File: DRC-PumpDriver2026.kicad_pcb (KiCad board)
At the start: 2 copper layers, 80 x 60 mm, 89 parts, among them J1 STLINK, J10 Vin_PWR, J2 CAN, J3 CAN, J4 PUMP1, J5 PUMP2, J6 PUMP3, J7 PUMP4, J8 PUMP5, J9 PUMP6, Q1 MTB7D0N6RJ3, Q2 MTB7D0N6RJ3, Q3 MTB7D0N6RJ3, Q4 MTB7D0N6RJ3, Q5 MTB7D0N6RJ3, Q6 MTB7D0N6RJ3, SW1 SW_Push, SW2 DIP, U1 AZ1084C-3.3, U2 STM32F303K8Tx, U3 SI-8050Y, U4 TLP2348, U5 TLP2348, U6 TLP2348, U7 TLP2348, U8 TLP2348, U9 TLP2348

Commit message: シルクスクリーンを修正
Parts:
- D5: value 5V -> POWER
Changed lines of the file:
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@@
 			)
 		)
-		(property "Value" "5V"
+		(property "Value" "POWER"
 			(at -1.919 0 270)
 			(unlocked yes)

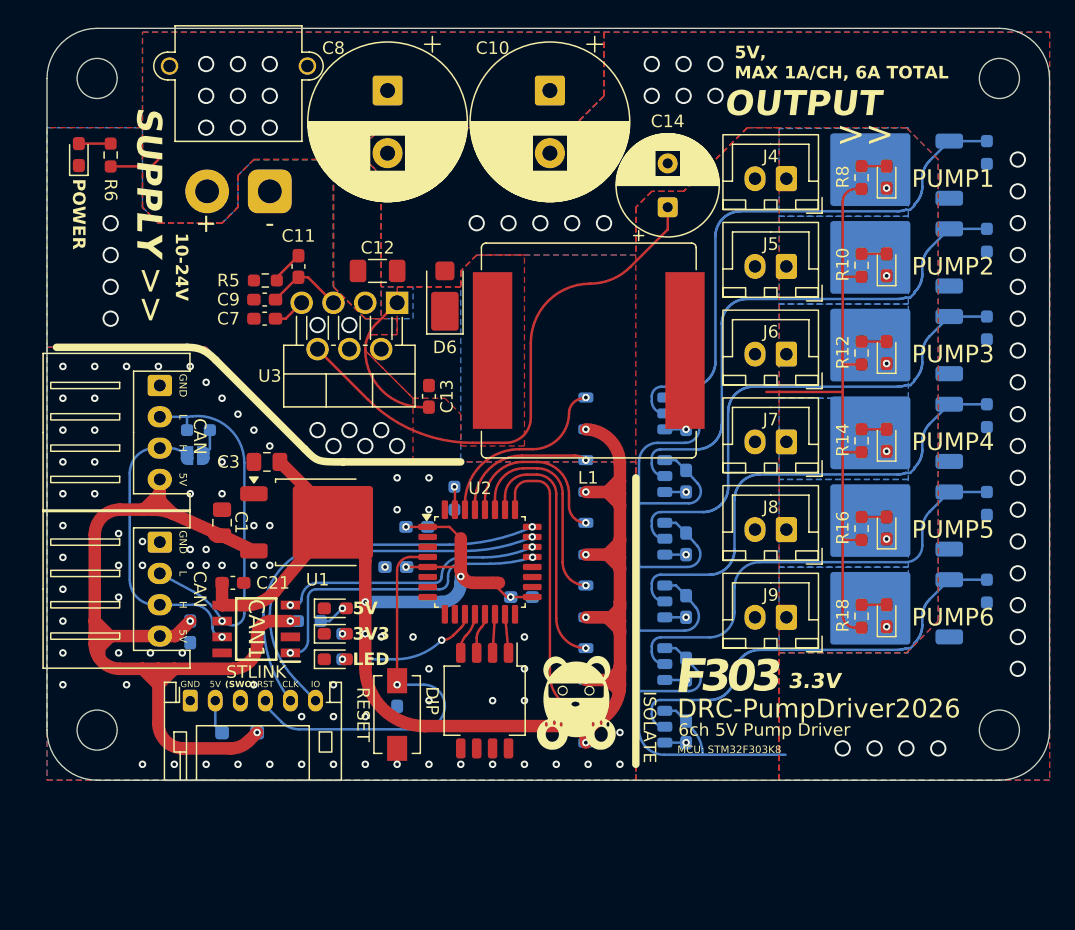
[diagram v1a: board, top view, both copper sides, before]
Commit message: 抜けてたフォトカプラの抵抗を追加
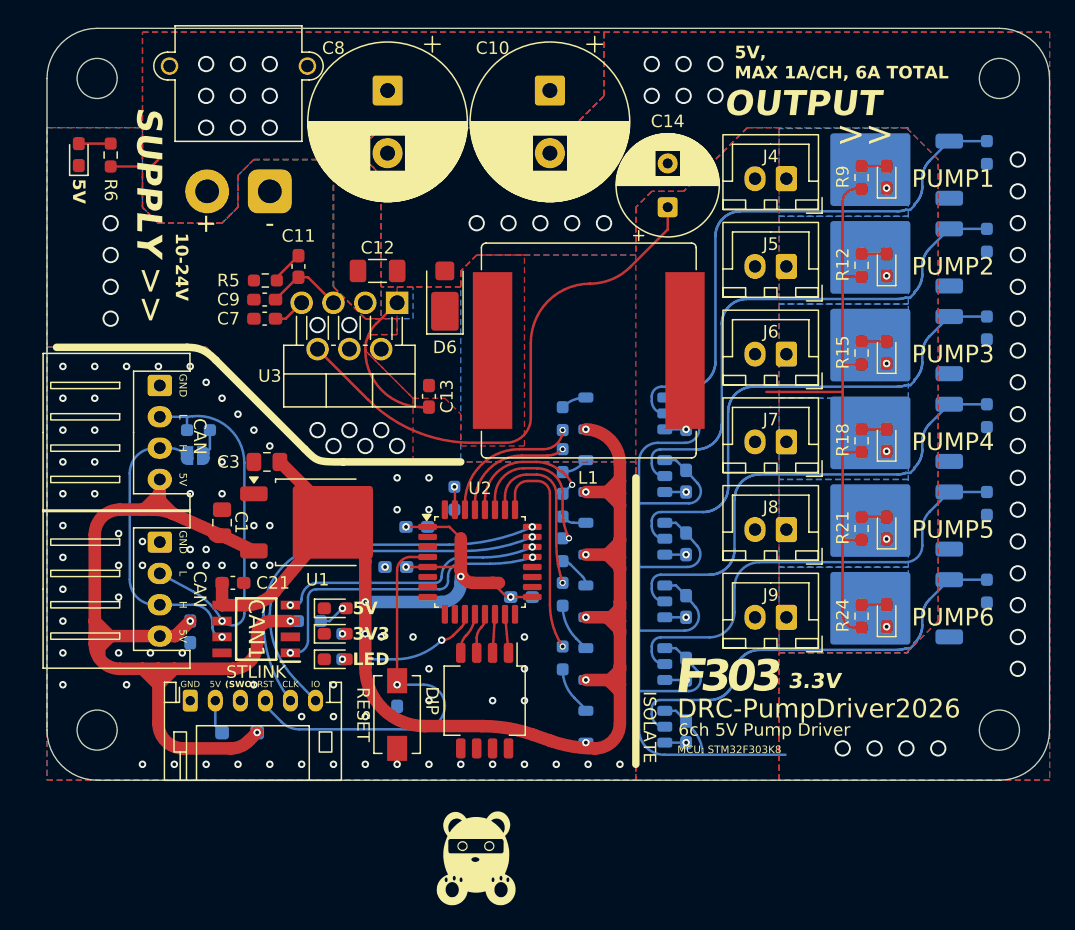
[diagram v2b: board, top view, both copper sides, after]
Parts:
- added R10: 560, Resistor_SMD:R_0603_1608Metric_Pad0.98x0.95mm_HandSolder, B.Cu at (154.2, 94.5)
- added R13: 560, Resistor_SMD:R_0603_1608Metric_Pad0.98x0.95mm_HandSolder, B.Cu at (154.2, 98.1)
- added R16: 560, Resistor_SMD:R_0603_1608Metric_Pad0.98x0.95mm_HandSolder, B.Cu at (154.2, 101.6)
- added R19: 560, Resistor_SMD:R_0603_1608Metric_Pad0.98x0.95mm_HandSolder, B.Cu at (154.2, 105.2)
- added R22: 560, Resistor_SMD:R_0603_1608Metric_Pad0.98x0.95mm_HandSolder, B.Cu at (154.2, 110.3)
- added R7: 560, Resistor_SMD:R_0603_1608Metric_Pad0.98x0.95mm_HandSolder, B.Cu at (154.2, 91.2)
- D5: value POWER -> 5V
- moved G*** 14.8 mm to (147.3, 126.4)
- renumbered R9 to R11, R10 to R12, R11 to R14, R12 to R15, R13 to R17, R14 to R18, R15 to R20, R16 to R21, R17 to R23, R18 to R24, R19 to R25, R7 to R8, R8 to R9
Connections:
- U4 pad 3: /PUMP1_EN -> Net-(U4-K)
- U5 pad 3: /PUMP2_EN -> Net-(U5-K)
- U6 pad 3: /PUMP3_EN -> Net-(U6-K)
- U7 pad 3: /PUMP4_EN -> Net-(U7-K)
- U8 pad 3: /PUMP5_EN -> Net-(U8-K)
- U9 pad 3: /PUMP6_EN -> Net-(U9-K)
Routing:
- net /PUMP6_EN: track 24.0 -> 17.5 mm
- net /PUMP5_EN: track 20.4 -> 14.0 mm
- net /PUMP4_EN: track 17.0 -> 12.3 mm
- net Net-(U8-K): track 0.00 -> 3.97 mm
- net Net-(U9-K): track 0.00 -> 3.91 mm
- net /PUMP1_EN: track 14.6 -> 11.4 mm
- net Net-(U7-K): track 0.00 -> 2.83 mm
- net /PUMP3_EN: track 13.5 -> 11.1 mm
- net Net-(U5-K): track 0.00 -> 2.14 mm
- net Net-(U4-K): track 0.00 -> 2.05 mm
- net Net-(U6-K): track 0.00 -> 2.01 mm
- net +3V3: track 135.0 -> 133.2 mm
- net /PUMP2_EN: track 11.5 -> 9.69 mm
- net GND: vias 80 -> 79
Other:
- board text added: "Designed by kotek, April 2026"
- board text removed: "Designed by kotek, March 2026"

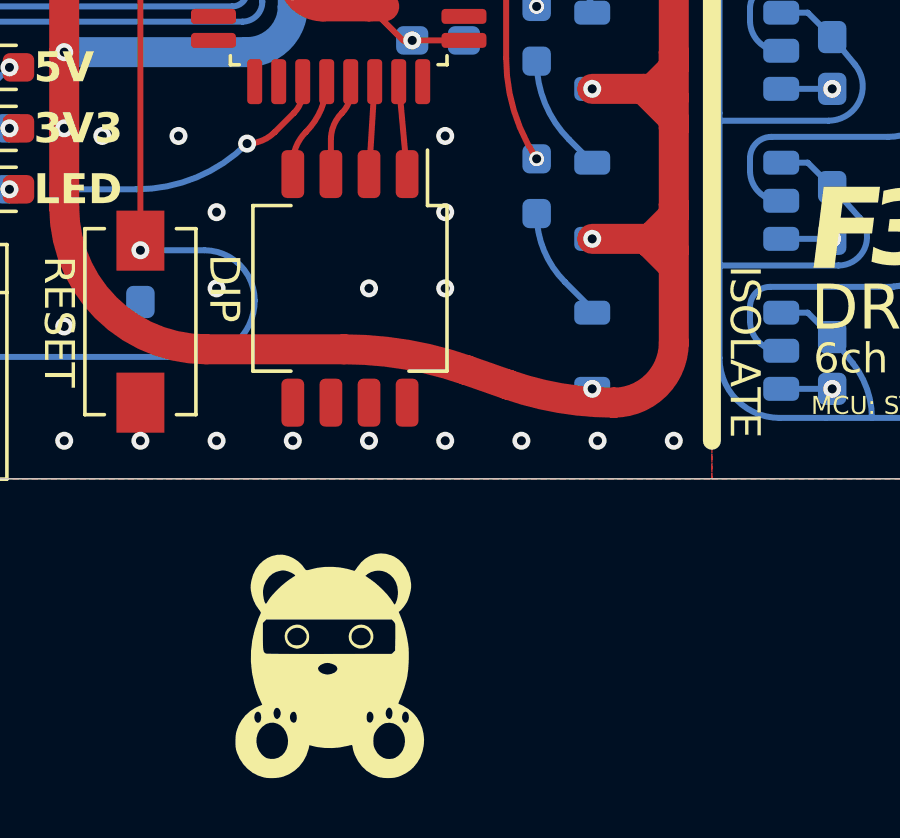
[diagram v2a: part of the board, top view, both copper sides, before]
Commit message: ロボクマのシルクスクリーンの位置を変更
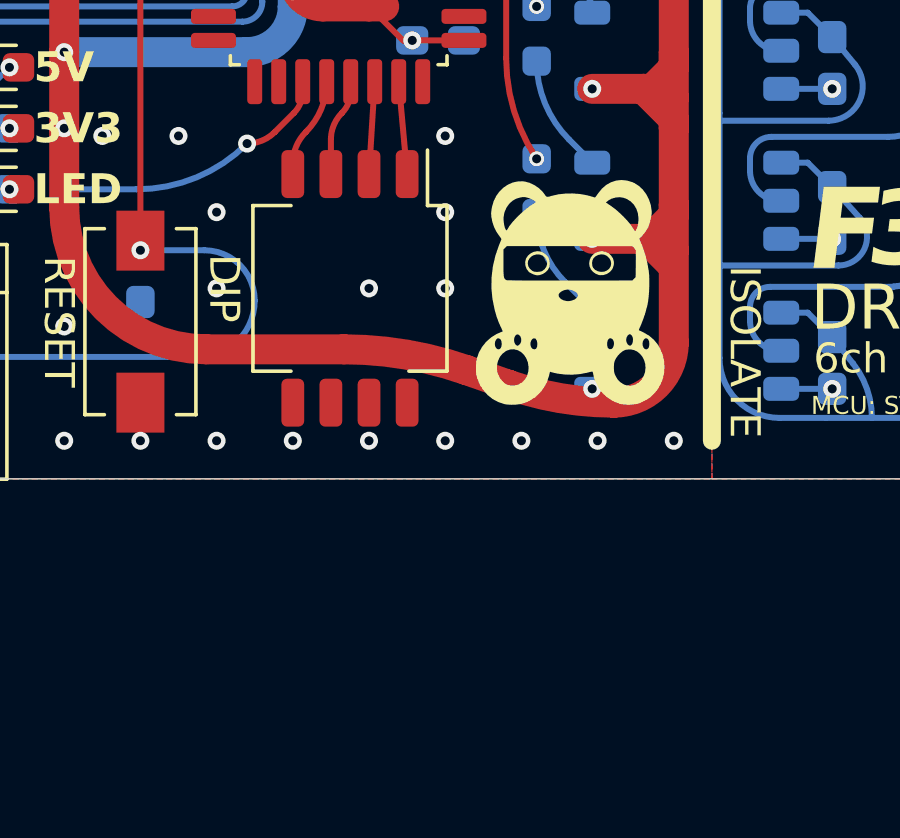
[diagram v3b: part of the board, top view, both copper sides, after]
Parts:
- moved G*** 14.8 mm to (155.3, 113.9)

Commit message: バージョン表記を追加
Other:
- board text added: "DRC-PumpDriver2026 v0.0.1"

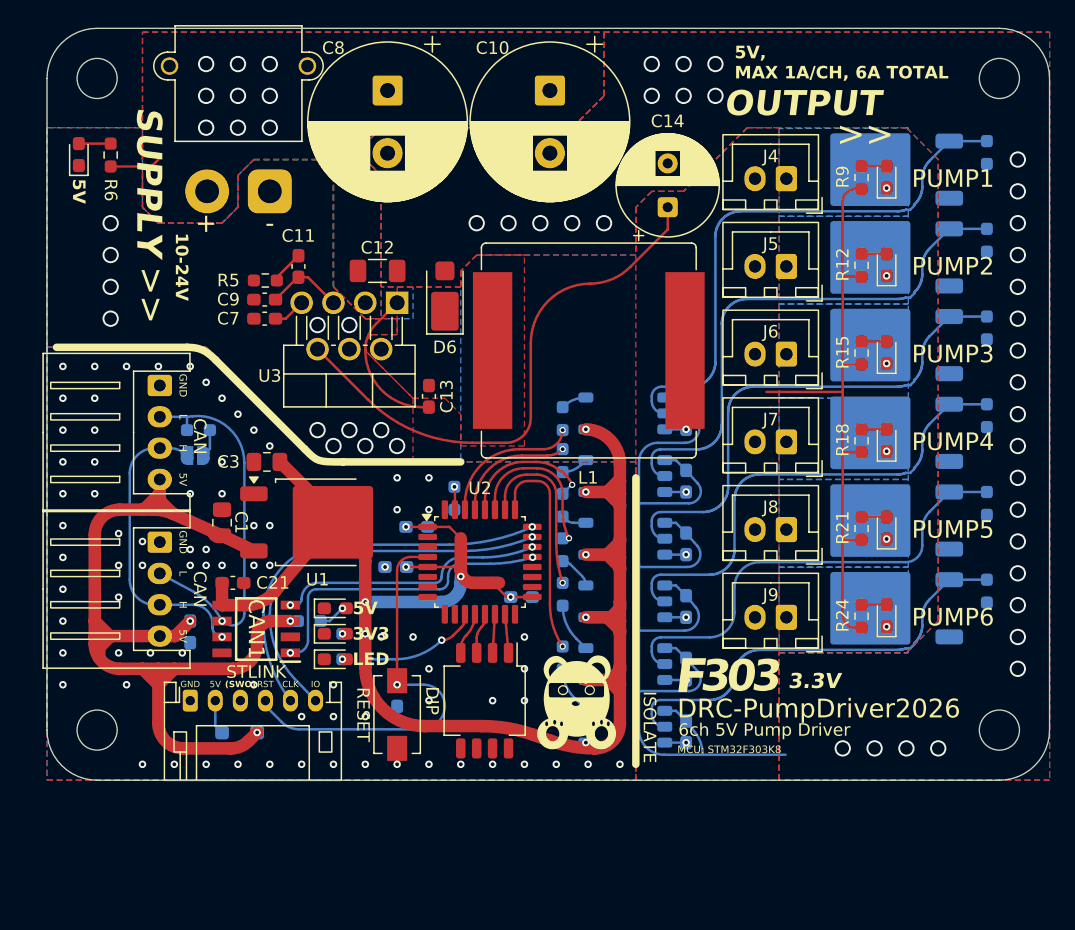
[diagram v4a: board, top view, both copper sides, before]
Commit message: DCDCを外して、電源入力に変更、v0.0.2
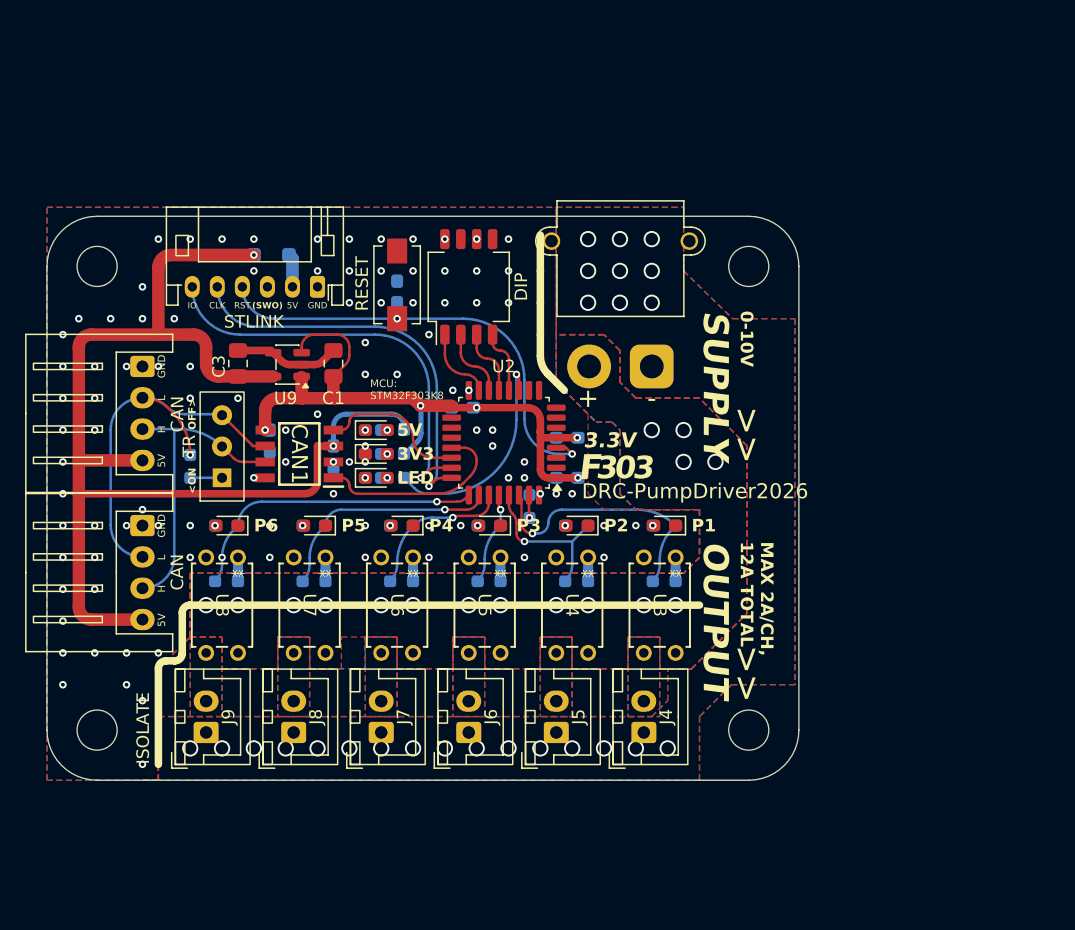
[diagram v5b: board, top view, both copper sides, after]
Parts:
- removed C10: 1000u/50V, Capacitor_THT:CP_Radial_D12.5mm_P5.00mm
- removed C11: 1200p, Capacitor_SMD:C_0603_1608Metric_Pad1.08x0.95mm_HandSolder
- removed C12: 4.7u/50V, Capacitor_SMD:C_1206_3216Metric_Pad1.33x1.80mm_HandSolder
- removed C13: 0.22u/50V, Capacitor_SMD:C_0603_1608Metric_Pad1.08x0.95mm_HandSolder
- removed C14: 470u/25V, Capacitor_THT:CP_Radial_D8.0mm_P3.50mm
- removed C15, C16, C17, C18, C19, C20: 0.1u, Capacitor_SMD:C_0603_1608Metric_Pad1.08x0.95mm_HandSolder
- removed the C7 at (130.4, 83.2)
- removed the C8 at (140.2, 65.0)
- removed C9: 680p, Capacitor_SMD:C_0603_1608Metric_Pad1.08x0.95mm_HandSolder
- removed the D5 at (115.6, 70.1)
- removed the D6 at (144.8, 81.4)
- removed JP1: TR, Jumper:SolderJumper-2_P1.3mm_Open_RoundedPad1.0x1.5mm
- removed L1: 56u, Inductor_SMD:L_Bourns_SRP1770TA_16.9x16.9mm
- removed Q1, Q2, Q3, Q4, Q5, Q6: MTB7D0N6RJ3, Package_TO_SOT_SMD:TO-252-2
- removed the R11 at (188.0, 76.9)
- removed the R14 at (188.0, 83.9)
- removed the R17 at (188.0, 90.9)
- removed R20, R23: 10k, Resistor_SMD:R_0603_1608Metric_Pad0.98x0.95mm_HandSolder
- removed the R5 at (130.5, 80.1)
- removed the R6 at (118.1, 70.1)
- removed the R8 at (188.0, 69.9)
- removed the REF** at (189.0, 116.0)
- removed the REF** at (117.0, 64.0)
- removed the REF** at (189.0, 64.0)
- removed U1: AZ1084C-3.3, Package_TO_SOT_SMD:TO-252-2
- added REF**: MountingHole_3.2mm_M3, MountingHole:MountingHole_3.2mm_M3, F.Cu at (117.0, 79.0)
- added REF**: MountingHole_3.2mm_M3, MountingHole:MountingHole_3.2mm_M3, F.Cu at (169.0, 79.0)
- added REF**: MountingHole_3.2mm_M3, MountingHole:MountingHole_3.2mm_M3, F.Cu at (169.0, 116.0)
- added SW3: SS-12D00G3, lib:SS-12D00G3, F.Cu at (127.0, 93.4)
- C1: value 10u -> 1u
- C3: value 22u -> 1u
- C7: renamed from C21; moved to B.Cu
- G***: moved to B.Cu
- J10: value Vin_PWR -> VIN_PWR
- R10: renamed from R13; value 560 -> 470
- R11: renamed from R18; value 10k -> 470; moved to B.Cu
- R12: renamed from R16; value 560 -> 470
- R13: renamed from R21; value 10k -> 470; moved to B.Cu
- R14: renamed from R19; value 560 -> 470
- R15: renamed from R24; value 10k -> 470; moved to B.Cu
- R16: renamed from R22; value 560 -> 470
- R5: renamed from R9; value 10k -> 470; moved to B.Cu
- R6: renamed from R7; value 560 -> 470
- R7: renamed from R12; value 10k -> 470; moved to B.Cu
- R8: renamed from R10; value 560 -> 470
- R9: renamed from R15; value 10k -> 470; moved to B.Cu
- U3: value SI-8050Y -> TLP241A; footprint Package_TO_SOT_THT:TO-220F-7_P2.54x3.7mm_StaggerOdd_Lead3.5mm_Vertical -> lib:DIP4_TOS
- U4, U5, U6, U7, U8: value TLP2348 -> TLP241A; footprint Package_SO:SO-5-6_4.55x3.7mm_P1.27mm -> lib:DIP4_TOS; moved to F.Cu
- U9: value TLP2348 -> RT9080-33GJ5; footprint Package_SO:SO-5-6_4.55x3.7mm_P1.27mm -> Package_TO_SOT_SMD:TSOT-23-5; moved to F.Cu
- moved D10 53.1 mm to (127.4, 99.7), turned to 180 degrees
- moved R15 51.2 mm to (127.4, 99.7), turned to 180 degrees
- moved REF** 50.1 mm to (135.9, 87.0)
- moved J9 47.2 mm to (125.7, 116.2), turned to 90 degrees
- moved D9 45.7 mm to (134.4, 99.7), turned to 180 degrees
- moved J4 45.6 mm to (160.7, 116.2), turned to 90 degrees
- moved R13 43.7 mm to (134.3, 99.7), turned to 180 degrees
- moved J8 42.5 mm to (132.7, 116.2), turned to 90 degrees
- moved J5 41.5 mm to (153.7, 116.2), turned to 90 degrees
- moved J7 39.8 mm to (139.7, 116.2), turned to 90 degrees
- moved U9 39.5 mm to (132.2, 86.8), turned to 180 degrees
- moved J6 39.4 mm to (146.7, 116.2), turned to 90 degrees
- moved D8 39.3 mm to (141.4, 99.7), turned to 180 degrees
- moved D1 38.2 mm to (130.9, 78.1), turned to 0 degrees
- moved R11 37.3 mm to (141.3, 99.7), turned to 180 degrees
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- renumbered C22 to C8, D12 to D10, D7 to D5, D8 to D6, D9 to D7, D10 to D8, D11 to D9, R25 to R17
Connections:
- C1 pad 1: +5V -> +3V3
- C3 pad 1: +3V3 -> +5V
- D10 pad 1: /PUMP6_SW -> GND
- D5 pad 1: /PUMP1_SW -> GND
- D6 pad 1: /PUMP2_SW -> GND
- D7 pad 1: /PUMP3_SW -> GND
- D8 pad 1: /PUMP4_SW -> GND
- D9 pad 1: /PUMP5_SW -> GND
- J4 pad 1: /PUMP1_SW -> GNDPWR
- J4 pad 2: +5VP -> /PUMP1_DRV
- J5 pad 1: /PUMP2_SW -> GNDPWR
- J5 pad 2: +5VP -> /PUMP2_DRV
- J6 pad 1: /PUMP3_SW -> GNDPWR
- J6 pad 2: +5VP -> /PUMP3_DRV
- J7 pad 1: /PUMP4_SW -> GNDPWR
- J7 pad 2: +5VP -> /PUMP4_DRV
- J8 pad 1: /PUMP5_SW -> GNDPWR
- J8 pad 2: +5VP -> /PUMP5_DRV
- J9 pad 1: /PUMP6_SW -> GNDPWR
- J9 pad 2: +5VP -> /PUMP6_DRV
- R10 pad 1: Net-(U6-K) -> Net-(R10-Pad1)
- R11 pad 1: +5VP -> /PUMP4_EN
- R12 pad 1: Net-(U7-K) -> Net-(R12-Pad1)
- R13 pad 1: +5VP -> /PUMP5_EN
- R14 pad 1: Net-(U8-K) -> Net-(R14-Pad1)
- R15 pad 1: +5VP -> /PUMP6_EN
- R16 pad 1: Net-(U9-K) -> Net-(R16-Pad1)
- R5 pad 1: +5VP -> /PUMP1_EN
- R6 pad 1: Net-(U4-K) -> Net-(R6-Pad1)
- R7 pad 1: +5VP -> /PUMP2_EN
- R8 pad 1: Net-(U5-K) -> Net-(R8-Pad1)
- R9 pad 1: +5VP -> /PUMP3_EN
- U3 pad 1: /BS -> Net-(R6-Pad1)
- U3 pad 2: /SW -> GND
- U3 pad 3: Vin_PWR -> /PUMP1_DRV
- U3 pad 4: GNDPWR -> Vin_PWR
- U4 pad 1: +3V3 -> Net-(R8-Pad1)
- U4 pad 3: Net-(U4-K) -> /PUMP2_DRV
- U4 pad 4: GNDPWR -> Vin_PWR
- U5 pad 1: +3V3 -> Net-(R10-Pad1)
- U5 pad 3: Net-(U5-K) -> /PUMP3_DRV
- U5 pad 4: GNDPWR -> Vin_PWR
- U6 pad 1: +3V3 -> Net-(R12-Pad1)
- U6 pad 3: Net-(U6-K) -> /PUMP4_DRV
- U6 pad 4: GNDPWR -> Vin_PWR
- U7 pad 1: +3V3 -> Net-(R14-Pad1)
- U7 pad 3: Net-(U7-K) -> /PUMP5_DRV
- U7 pad 4: GNDPWR -> Vin_PWR
- U8 pad 1: +3V3 -> Net-(R16-Pad1)
- U8 pad 3: Net-(U8-K) -> /PUMP6_DRV
- U8 pad 4: GNDPWR -> Vin_PWR
- U9 pad 3: Net-(U9-K) -> +3V3
- U9 pad 4: GNDPWR -> GND
- U9 pad 5: Net-(Q6-G) -> +5V
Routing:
- net +5VP: track 106.9 -> 0.00 mm, vias 6 -> 0
- net GNDPWR: track 87.1 -> 0.00 mm, vias 44 -> 25
- net +3V3: track 133.2 -> 51.2 mm, vias 12 -> 5
- net Net-(Q1-G): track 44.9 -> 0.00 mm
- net Net-(Q2-G): track 42.9 -> 0.00 mm
- net Net-(Q3-G): track 40.9 -> 0.00 mm
- net Net-(Q4-G): track 38.9 -> 0.00 mm
- net Net-(Q5-G): track 37.1 -> 0.00 mm
- net Net-(Q6-G): track 35.0 -> 0.00 mm
- net +5V: track 78.5 -> 95.5 mm, vias 3 -> 2
- net /BS: track 12.2 -> 0.00 mm
- net /PUMP1_EN: track 11.4 -> 21.3 mm
- net /CAN_RX: track 21.4 -> 12.0 mm, vias 2 -> 0
- net /CAN_TX: track 24.9 -> 16.0 mm, vias 2 -> 0
- net GND: track 0.00 -> 8.46 mm, vias 79 -> 104
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- added copper zone on B.Cu, net /PUMP1_DRV
- added copper zone on F.Cu, net /PUMP1_DRV
- added copper zone on B.Cu, net /PUMP2_DRV
- added copper zone on F.Cu, net /PUMP2_DRV
- added copper zone on B.Cu, net /PUMP3_DRV
- added copper zone on F.Cu, net /PUMP3_DRV
- added copper zone on B.Cu, net /PUMP4_DRV
- added copper zone on F.Cu, net /PUMP4_DRV
- added copper zone on B.Cu, net /PUMP5_DRV
- added copper zone on F.Cu, net /PUMP5_DRV
- added copper zone on B.Cu, net /PUMP6_DRV
- added copper zone on F.Cu, net /PUMP6_DRV
- removed copper zone on F.Cu, net +5VP
- removed copper zone on B.Cu, net /PUMP1_SW
- removed copper zone on B.Cu, net /PUMP2_SW
- removed copper zone on B.Cu, net /PUMP3_SW
- removed copper zone on B.Cu, net /PUMP4_SW
- removed copper zone on B.Cu, net /PUMP5_SW
- removed copper zone on B.Cu, net /PUMP6_SW
- removed copper zone on F.Cu, net /SW
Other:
- board size 80 x 60 mm -> 60 x 45 mm
- board text added: "*"
- board text added: "0-10V"
- board text added: "6ch Pump Driver"
- board text added: "<ON"
- board text added: "DRC-PumpDriver2026 v0.0.2"
- board text added: "MAX 2A/CH, 12A TOTAL"
- board text added: "OFF>"
- board text added: "P1"
- board text added: "P2"
- board text added: "P3"
- board text added: "P4"
- board text added: "P5"
- board text added: "P6"
- board text added: "TR"
- board text removed: "10-24V"
- board text removed: "5V, MAX 1A/CH, 6A TOTAL"
- board text removed: "6ch 5V Pump Driver"
- board text removed: "DRC-PumpDriver2026 v0.0.1"
- board text removed: "PUMP1"
- board text removed: "PUMP2"
- board text removed: "PUMP3"
- board text removed: "PUMP4"
- board text removed: "PUMP5"
- board text removed: "PUMP6"
